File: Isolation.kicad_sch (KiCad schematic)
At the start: 9 parts

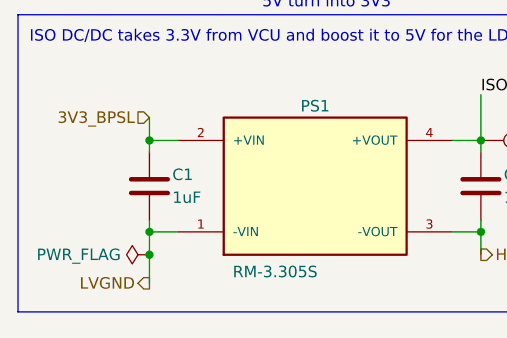
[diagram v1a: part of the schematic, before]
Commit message: added DE1a-12V precharge relay
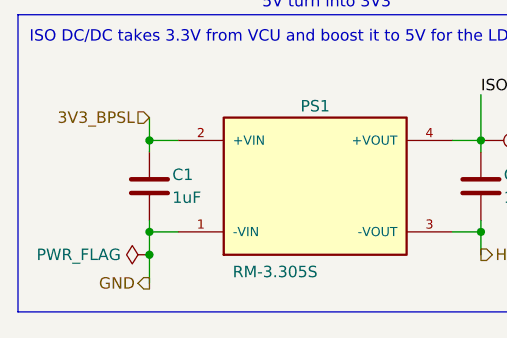
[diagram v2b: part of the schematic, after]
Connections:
- net LVGND renamed GND
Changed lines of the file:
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@@
 		)
 	)
-	(hierarchical_label "LVGND"
+	(hierarchical_label "GND"
 		(shape output)
 		(at 35.56 52.07 180)

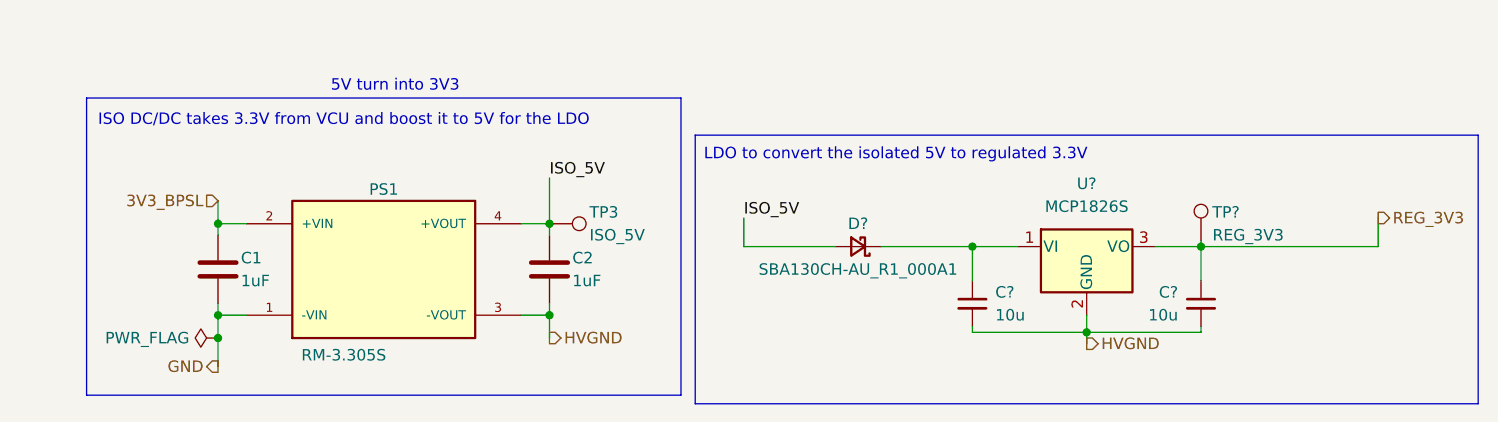
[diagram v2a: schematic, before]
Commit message: V_OUT_BAT & V_OUT_MOT & PRECHARGE_CTRL to MCU
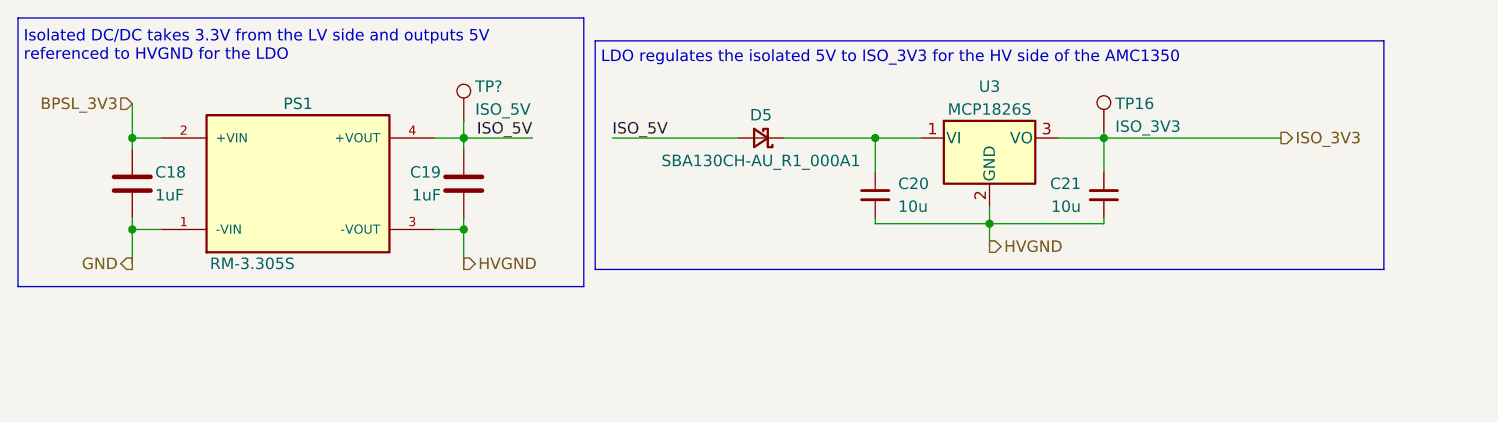
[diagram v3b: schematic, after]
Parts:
- removed TP3: ISO_5V, symbol Connector:TestPoint
- added TP?: ISO_5V, TestPoint:TestPoint_Loop_D1.80mm_Drill1.0mm_Beaded, symbol lhrs_misc:Multimeter_TP
- TP16: renamed from TP?; value REG_3V3 -> ISO_3V3
- gave numbers to parts that had none: 4
- renumbered C1 to C18, C2 to C19
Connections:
- net ISO_5V: now also TP?.1
- net 3V3_BPSL renamed BPSL_3V3
- net REG_3V3 renamed ISO_3V3
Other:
- note added: "Isolated DC/DC takes 3.3V from the LV side and outputs 5V referenced to HVGND for the LDO"
- note added: "LDO regulates the isolated 5V to ISO_3V3 for the HV side of the AMC1350"
- note removed: "5V turn into 3V3"
- note removed: "ISO DC/DC takes 3.3V from VCU and boost it to 5V for the LDO"
- note removed: "LDO to convert the isolated 5V to regulated 3.3V"
- moved on the sheet: C18, C19, C20, C21, D5, PS1, TP16, U3

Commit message: precharges & voltage sensors
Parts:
- added U5: EL3H7, LHRS_ICs:EL3H7, symbol lhrs_ics:EL3H7
- gave numbers to parts that had none: 1
- renumbered C18 to C24, C19 to C25, C20 to C26, C21 to C27, D5 to D1, U3 to U4
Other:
- note added: "Just go straight 5V no need for LDO"
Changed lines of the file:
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@@
+		)
+	)
+	(text "Just go straight 5V no need for LDO"
+		(exclude_from_sim no)
+		(at 94.615 46.355 0)
+		(effects
+			(font
+				(size 1.27 1.27)
+			)
 		)
 	)
@@
 		(in_pos_files yes)
 		(dnp no)
-		(property "Reference" "D5"
+		(property "Reference" "D1"
 			(at 95.885 24.13 0)
 			(show_name no)
@@
 			(project "PS-PrechargeBoard"
 				(path "/74d17fe6-68d4-4bd7-954a-e2bbb58b1f1e/1eddab22-6734-4f8a-8dd2-45ad51a5d964"
-					(reference "D5")
+					(reference "D1")
 					(unit 1)
 				)
@@
 		(in_pos_files yes)
 		(dnp no)
-		(property "Reference" "C18"
+		(property "Reference" "C24"
 			(at 28.575 30.48 0)
 			(show_name no)
@@
 			(project "PS-PrechargeBoard"
 				(path "/74d17fe6-68d4-4bd7-954a-e2bbb58b1f1e/1eddab22-6734-4f8a-8dd2-45ad51a5d964"
-					(reference "C18")
+					(reference "C24")
 					(unit 1)
 				)
@@
 		(in_pos_files yes)
 		(dnp no)
-		(property "Reference" "C21"
+		(property "Reference" "C27"
 			(at 131.445 31.75 0)
 			(show_name no)
@@
 			(project "PS-PrechargeBoard"
 				(path "/74d17fe6-68d4-4bd7-954a-e2bbb58b1f1e/1eddab22-6734-4f8a-8dd2-45ad51a5d964"
-					(reference "C21")
+					(reference "C27")
 					(unit 1)
 				)
@@
 		(in_pos_files yes)
 		(dnp no)
-		(property "Reference" "C20"
+		(property "Reference" "C26"
 			(at 111.125 31.75 0)
 			(show_name no)
@@
 			(project "PS-PrechargeBoard"
 				(path "/74d17fe6-68d4-4bd7-954a-e2bbb58b1f1e/1eddab22-6734-4f8a-8dd2-45ad51a5d964"
-					(reference "C20")
+					(reference "C26")
 					(unit 1)
 				)
@@
 		(in_pos_files yes)
 		(dnp no)
-		(property "Reference" "C19"
+		(property "Reference" "C25"
 			(at 60.325 30.48 0)
 			(show_name no)
@@
 			(project "PS-PrechargeBoard"
 				(path "/74d17fe6-68d4-4bd7-954a-e2bbb58b1f1e/1eddab22-6734-4f8a-8dd2-45ad51a5d964"
-					(reference "C19")
+					(reference "C25")
 					(unit 1)
 				)
@@
 		(in_pos_files yes)
 		(dnp no)
-		(property "Reference" "TP?"
+		(property "Reference" "TP15"
 			(at 64.135 20.955 0)
 			(show_name no)
@@
 			(project "PS-PrechargeBoard"
 				(path "/74d17fe6-68d4-4bd7-954a-e2bbb58b1f1e/1eddab22-6734-4f8a-8dd2-45ad51a5d964"
-					(reference "TP?")
+					(reference "TP15")
+					(unit 1)
+				)
+			)
+		)
+	)
+	(symbol
+		(lib_id "lhrs_ics:EL3H7")
+		(at 186.69 28.575 0)
+		(unit 1)
+		(body_style 1)
+		(exclude_from_sim no)
+		(in_bom yes)
+		(on_board yes)
+		(in_pos_files yes)
+		(dnp no)
+		(fields_autoplaced yes)
+		(property "Reference" "U5"
+			(at 186.69 19.685 0)
+			(show_name no)
+			(do_not_autoplace no)
+			(effects
+				(font
+					(size 1.27 1.27)
+				)
+			)
+		)
+		(property "Value" "EL3H7"
+			(at 186.69 22.225 0)
+			(show_name no)
+			(do_not_autoplace no)
+			(effects
+				(font
+					(size 1.27 1.27)
+				)
+			)
+		)
+		(property "Footprint" "LHRS_ICs:EL3H7"
+			(at 186.69 36.195 0)
+			(hide yes)
+			(show_name no)
+			(do_not_autoplace no)
+			(effects
+				(font
+					(size 1.27 1.27)
+				)
+			)
+		)
+		(property "Datasheet" "https://www.digikey.com/en/products/detail/everlight-electronics-co-ltd/EL3H7-D-TA-VG/2692979"
+			(at 186.69 29.845 0)
+			(hide yes)
+			(show_name no)
+			(do_not_autoplace no)
+			(effects
+				(font
+					(size 1.27 1.27)
+				)
+				(justify left)
+			)
+		)
+		(property "Description" "OPTOISO 3.75KV 1CH TRANS 4-SSOP"
+			(at 186.69 28.575 0)
+			(hide yes)
+			(show_name no)
+			(do_not_autoplace no)
+			(effects
+				(font
+					(size 1.27 1.27)
+				)
+			)
+		)
+		(property "P/N" "EL3H7(D)(TA)-VG"
+			(at 186.69 28.575 0)
+			(hide yes)
+			(show_name no)
+			(do_not_autoplace no)
+			(effects
+				(font
+					(size 1.27 1.27)
+				)
+			)
+		)
+		(property "Vf" "1.4V"
+			(at 186.69 28.575 0)
+			(hide yes)
+			(show_name no)
+			(do_not_autoplace no)
+			(effects
+				(font
+					(size 1.27 1.27)
+				)
+			)
+		)
+		(property "If" "20mA"
+			(at 186.69 28.575 0)
+			(hide yes)
+			(show_name no)
+			(do_not_autoplace no)
+			(effects
+				(font
+					(size 1.27 1.27)
+				)
+			)
+		)
+		(pin "3"
+		)
+		(pin "2"
+		)
+		(pin "1"
+		)
+		(pin "4"
+		)
+		(instances
+			(project "PS-PrechargeBoard"
+				(path "/74d17fe6-68d4-4bd7-954a-e2bbb58b1f1e/1eddab22-6734-4f8a-8dd2-45ad51a5d964"
+					(reference "U5")
 					(unit 1)
 				)
@@
 		(in_pos_files yes)
 		(dnp no)
-		(property "Reference" "U3"
+		(property "Reference" "U4"
 			(at 121.285 20.955 0)
 			(show_name no)
@@
 			(project "PS-PrechargeBoard"
 				(path "/74d17fe6-68d4-4bd7-954a-e2bbb58b1f1e/1eddab22-6734-4f8a-8dd2-45ad51a5d964"
-					(reference "U3")
+					(reference "U4")
 					(unit 1)
 				)

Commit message: saving
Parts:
- removed C26, C27: 10u, Capacitor_SMD:C_0805_2012Metric_Pad1.18x1.45mm_HandSolder, symbol Device:C_Small
- removed D1: SBA130CH-AU_R1_000A1, Diode_SMD:D_SOD-323_HandSoldering, symbol Device:D_Schottky_Small
- removed TP16: ISO_3V3, TestPoint:TestPoint_Loop_D1.80mm_Drill1.0mm_Beaded, symbol lhrs_misc:Multimeter_TP
- removed U4: MCP1826S, Package_TO_SOT_SMD:SOT-223-3_TabPin2, symbol Regulator_Linear:MCP1826S
- removed U5: EL3H7, LHRS_ICs:EL3H7, symbol lhrs_ics:EL3H7
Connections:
- net BPSL_3V3 renamed 3V3
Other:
- note removed: "Just go straight 5V no need for LDO"
- note removed: "LDO regulates the isolated 5V to ISO_3V3 for the HV side of the AMC1350"

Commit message: final schematic REV-A?
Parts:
- added R50: 500, symbol Device:R
- added R51: 5k, symbol Device:R
- added U3: EL3H7, LHRS_ICs:EL3H7, symbol lhrs_ics:EL3H7
- renumbered C24 to C31, C25 to C32, TP15 to TP23
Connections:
- net GND: now also U3.2
- net HVGND: now also R51.1
- net ISO_5V: now also U3.4
- new net: R50.2, U3.1
- new net HV_PRECHARGE_CTRL: R51.2, U3.3
- new net PRECHARGE_CTRL: R50.1
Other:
- note added: "(3.3 V − 1.2 V) / 5 mA = 420 ohms"
- note added: "4.8 V / (4.2 mA x 0.5) = 2.3k ohms"
- note added: "LED R: (drive voltage − LED forward voltage) / LED current"
- note added: "OUTPUT R: desired output voltage / (LED current x current transfer ratio) = minimum R"
- note added: "Optocoupler isolates the precharge command from LV to HV (non-inverting)"
- note added: "using 500 ohms R: (3.3 V − 1.2 V) / 500 ohms = 4.2 mA"
- note added: "using 5k ohms: 2.1 mA x 5 kohms = 10.5 V (more than 4.8 V, so output should reach full)"
- moved on the sheet: C31, C32, PS1, TP23

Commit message: main isolation & motor isolation
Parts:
- R50, R51: footprint (none) -> Package_DIP:DIP-8_W7.62mm
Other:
- moved on the sheet: C31, C32, PS1, R50, R51, TP23, U3

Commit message: removed isolation for AMC3311
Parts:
- added C60: 100p, Capacitor_SMD:C_0603_1608Metric_Pad1.08x0.95mm_HandSolder, symbol Device:C
- added C61, C64, C66, C? (x3): 1n, Capacitor_SMD:C_0603_1608Metric_Pad1.08x0.95mm_HandSolder, symbol Device:C
- added C62, C63, C65, C? (x3): 100n, Capacitor_SMD:C_0603_1608Metric_Pad1.08x0.95mm_HandSolder, symbol Device:C
- added C67, C?: 1u, Capacitor_SMD:C_0603_1608Metric_Pad1.08x0.95mm_HandSolder, symbol Device:C
- added C68: 10n, Capacitor_SMD:C_0603_1608Metric_Pad1.08x0.95mm_HandSolder, symbol Device:C
- added C?: 1uF, symbol Device:C
- added R57, R58, R59: 500k, Resistor_SMD:R_0805_2012Metric_Pad1.20x1.40mm_HandSolder, symbol Device:R
- added R60: 20k, Resistor_SMD:R_0603_1608Metric_Pad0.98x0.95mm_HandSolder, symbol Device:R
- added R61: 47k, Resistor_SMD:R_0603_1608Metric_Pad0.98x0.95mm_HandSolder, symbol Device:R
- added R62, R63: 10, Resistor_SMD:R_0603_1608Metric_Pad0.98x0.95mm_HandSolder, symbol Device:R
- added R? (x4): 100k, Package_DIP:DIP-8_W7.62mm, symbol Device:R
- added R?: 10k, Package_DIP:DIP-8_W7.62mm, symbol Device:R
- added TP?: V_IN+, TestPoint:TestPoint_Loop_D1.80mm_Drill1.0mm_Beaded, symbol lhrs_misc:Multimeter_TP
- added U8, U?: AMC3311QDWERQ1, AMC3311QDWERQ1:DWE0016A-IPC_A, symbol AMC3311QDWERQ1:AMC3311QDWERQ1
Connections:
- net GND is gone; now on net 3V3: C31.2, PS1.1 (-VIN), U3.2
- net 3V3: now also C65.2, C66.2, C67.2, C?.1, C?.2, C?.2, U8.15 (DCDC_GND), U8.9 (GND), U?.9 (GND)
- net HVGND: now also C?.1, C?.1, C?.1, C?.2, C?.2, R?.2, U?.15 (DCDC_GND), U?.2 (DCDC_HGND), U?.7 (HGND), U?.8 (HGND)
- new net: R?.1, R?.2 (x3)
- new net: R57.2, R58.1
- new net: R58.2, R59.1
- new net: C63.2, C64.2, U8.5 (HLDO_OUT)
- new net: C60.1, R59.2, R60.2, U8.6 (IN)
- new net: C65.1, U8.13 (LDO_OUT), U8.16 (DCDC_IN)
- new net: C61.1, C62.2, U8.1 (DCDC_OUT), U8.3 (HLDO_IN)
- new net: R62.1, U8.11 (OUTP)
- new net: R63.1, U8.10 (OUTN)
- new net +3v3: C66.1, C67.1, R61.1, U8.12 (VDD)
- new net DCDC_IN: C?.2, U?.13 (LDO_OUT), U?.16 (DCDC_IN)
- new net DCDC_OUT: C?.1, C?.2, U?.1 (DCDC_OUT), U?.3 (HLDO_IN)
- new net DIAG: U?.14 (DIAG)
- new net DIAG Pin: R61.2, U8.14 (DIAG)
- new net HLDO_OUT: C?.2, C?.2, U?.5 (HLDO_OUT)
- new net HV GND: C60.2, C61.2, C62.1, C63.1, C64.1, R60.1, U8.2 (DCDC_HGND), U8.7 (HGND), U8.8 (HGND)
- new net HV+: R?.1
- new net Input: R57.1
- new net OUTN: U?.10 (OUTN)
- new net OUTP: U?.11 (OUTP)
- new net OUT_N: C68.1, R63.2
- new net OUT_P: C68.2, R62.2
- new net VDD: C?.1, C?.1, U?.12 (VDD)
- new net V_IN+: C?.1, R?.1, R?.2, TP?.1, U?.6 (IN)
- no-connect marks 0 -> 2
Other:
- note added: "HV divider scales HV+ (100V-130V)down to V_IN (max 3.17V) for isolated amplifier"
